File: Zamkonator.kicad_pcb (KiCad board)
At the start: 2 copper layers, 75 x 75 mm, 126 parts, among them J1 Screw_Terminal_01x06, J3 Conn_01x08_Male, J4 Conn_02x06_Counter_Clockwise, J5 Conn_01x04_Female, J6 Conn_01x03_Female, K1 SRD-DC3V-SL-C, Q1 BCP56, T1 HR051142, U1 RTL8201F, U2 SI3404-A-GM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

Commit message: Kicad updates, added missing resistances
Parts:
- C18: value C -> 100n 100V
- C21: value C -> 1n 100V
- R16: value R -> 130K
- R18: value R -> 0
- moved Q1 0.35 mm to (11.0, 27.6)
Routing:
- net Net-(U1-MDI0+): track 28.7 -> 26.2 mm

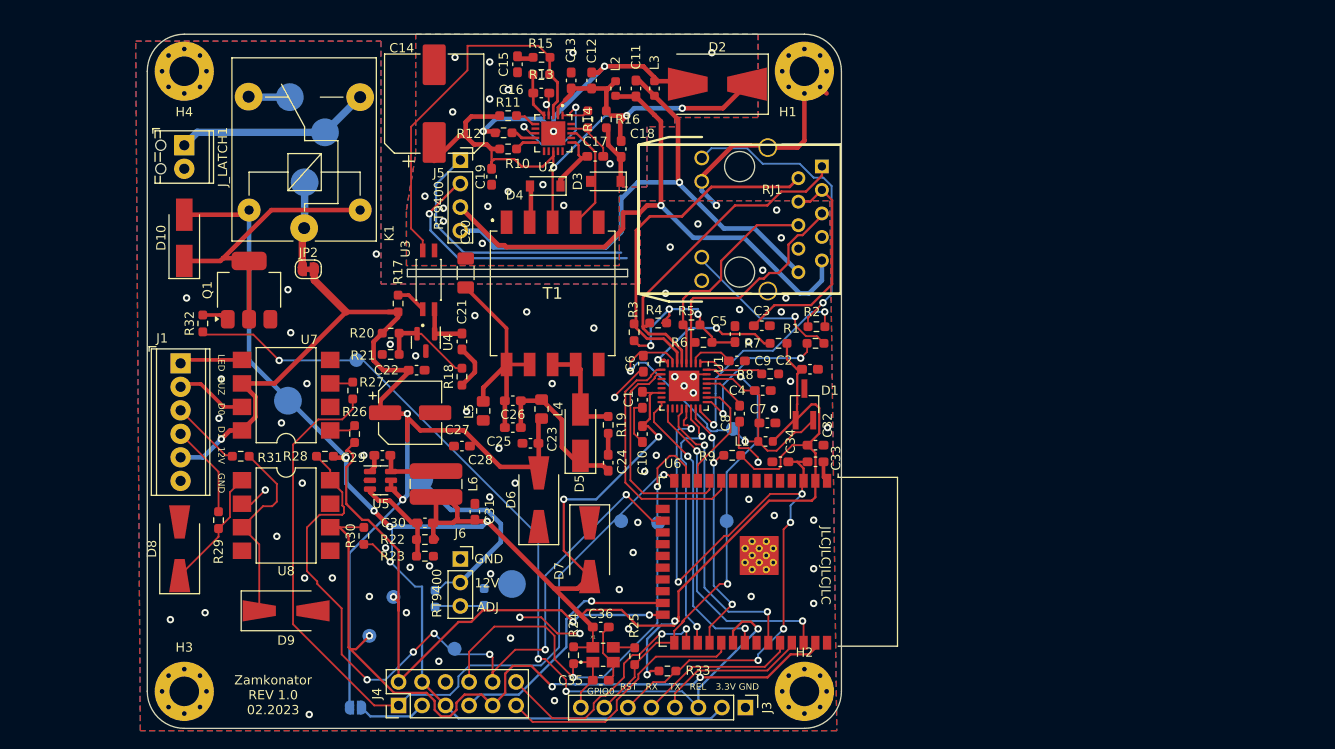
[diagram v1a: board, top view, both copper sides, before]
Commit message: Update schematic for V1.1
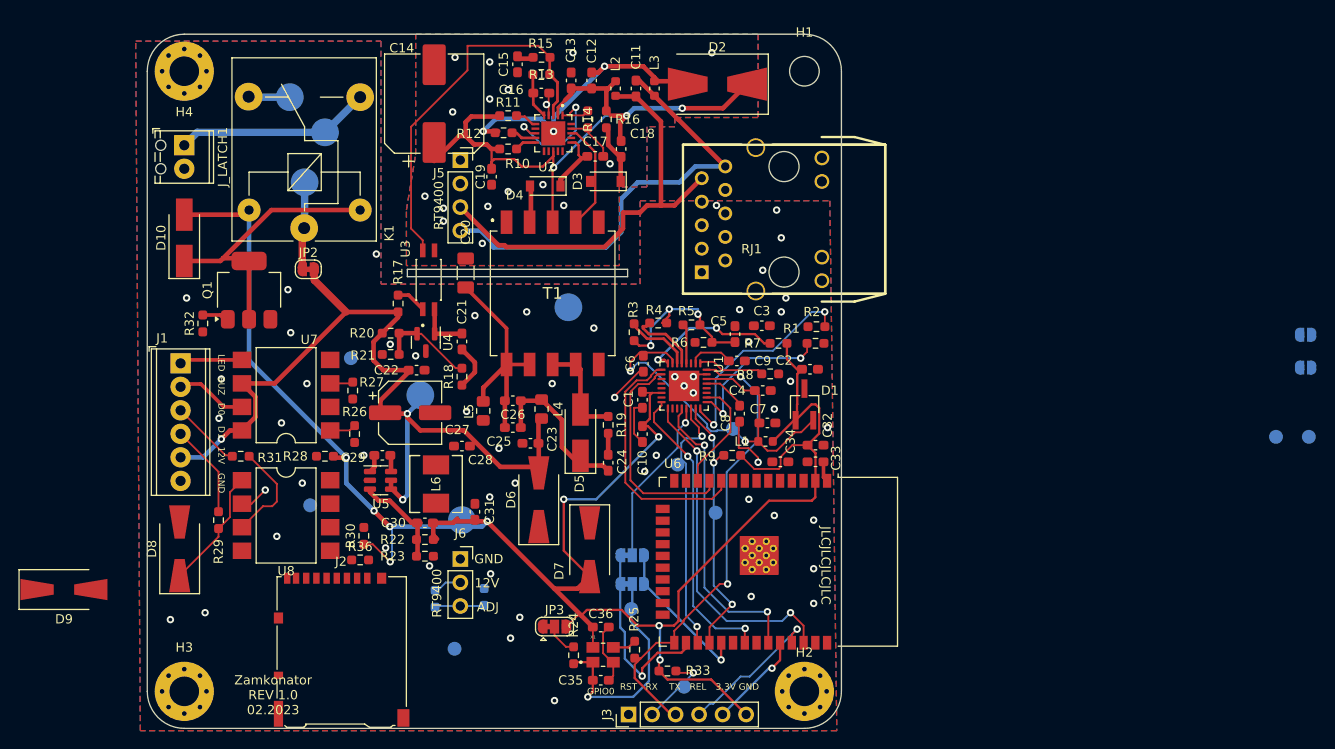
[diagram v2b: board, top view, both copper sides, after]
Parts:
- removed J4: Conn_02x06_Counter_Clockwise, Connector_PinHeader_2.54mm:PinHeader_2x06_P2.54mm_Vertical
- removed JP1: SolderJumper_2_Open, Jumper:SolderJumper-2_P1.3mm_Open_RoundedPad1.0x1.5mm
- added J2: Micro_SD_Card_Det1, Connector_Card:microSD_HC_Hirose_DM3AT-SF-PEJM5, F.Cu at (21.0, 66.5)
- added JP3: CLK_EN pull, Jumper:SolderJumper-3_P1.3mm_Bridged12_RoundedPad1.0x1.5mm, F.Cu at (44.0, 64.0)
- added JP4: EMAC_EN_JUMPER, Jumper:SolderJumper-3_P1.3mm_Bridged12_RoundedPad1.0x1.5mm, B.Cu at (52.4, 56.3)
- added JP5: CLK_EN_JUMPER, Jumper:SolderJumper-3_P1.3mm_Bridged12_RoundedPad1.0x1.5mm, B.Cu at (52.4, 59.4)
- added JP6: SolderJumper_2_Open, Jumper:SolderJumper-2_P1.3mm_Open_RoundedPad1.0x1.5mm, B.Cu at (125.2, 32.5)
- added JP7: SolderJumper_2_Open, Jumper:SolderJumper-2_P1.3mm_Open_RoundedPad1.0x1.5mm, B.Cu at (125.2, 36.0)
- added R36: 10k, Resistor_SMD:R_0603_1608Metric_Pad0.98x0.95mm_HandSolder, F.Cu at (23.0, 56.8)
- added TP15: EMAC_MDC, TestPoint:TestPoint_Pad_D1.5mm, B.Cu at (57.3, 46.5)
- added TP16: EMAC_MDIO, TestPoint:TestPoint_Pad_D1.5mm, B.Cu at (61.4, 51.7)
- H1: footprint MountingHole:MountingHole_3.2mm_M3_Pad_Via -> MountingHole:MountingHole_3.2mm_M3
- J3: footprint Connector_PinHeader_2.54mm:PinHeader_1x08_P2.54mm_Vertical -> Connector_PinHeader_2.54mm:PinHeader_1x06_P2.54mm_Vertical
- L6: value SWPA6045S6R8MT -> ETQP3M6R8KVP; footprint SWPA6045S6R8MT:SWPA6045S6R8MT -> panasonic_coil:IND_PCC-M0530M-LP_PAN
- R11: value 24.3 1% -> 24.3k 1%
- TP1: value TestPoint -> GND
- TP10: value TestPoint -> DAT0_INV
- TP11: value TestPoint -> LED_CTL
- TP12: value TestPoint -> R_NO
- TP13: value TestPoint -> R_NC
- TP14: value TestPoint -> R_C
- TP2: value TestPoint -> +12V
- TP3: value TestPoint -> ESP_EN
- TP4: value TestPoint -> RELAY_CTL
- TP5: value TestPoint -> PHY_AVDD
- TP6: value TestPoint -> +3.3V
- TP7: value TestPoint -> CLK_EN
- TP8: value TestPoint -> BUZZER_CTL
- TP9: value TestPoint -> DAT1_INV
- moved TP4 103.2 mm to (125.5, 43.5)
- moved TP11 100.3 mm to (122.0, 43.5)
- moved TP8 34.1 mm to (22.0, 35.0)
- moved TP1 30.5 mm to (45.5, 29.5)
- moved D9 24.1 mm to (-9.00, 60.0)
- moved TP6 22.8 mm to (34.0, 52.5)
- moved TP3 18.5 mm to (58.0, 70.5)
- moved TP10 13.4 mm to (17.6, 50.9)
- moved J3 12.6 mm to (52.0, 73.5), turned to 90 degrees
- moved TP7 9.74 mm to (52.3, 62.1)
- moved TP2 9.00 mm to (29.5, 39.0)
- moved R25 0.70 mm to (52.7, 66.5)
- turned RJ1 to 180 degrees
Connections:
- net /ESP32/EMAC_CRS_DV renamed /EMAC_CRS_DV
- net /ESP32/EMAC_MDC renamed /EMAC_MDC
- net /ESP32/EMAC_MDIO renamed /EMAC_MDIO
- net /ESP32/EMAC_RXD0 renamed /EMAC_RXD0
- net /ESP32/EMAC_RXD1 renamed /EMAC_RXD1
- net /ESP32/EMAC_TXD0 renamed /EMAC_TXD0
- net /ESP32/EMAC_TXD1 renamed /EMAC_TXD1
- net /ESP32/EMAC_TX_EN renamed /EMAC_TX_EN
- net /ESP32/IO12 renamed /BUZ_CTL
- net /ESP32/RX renamed /ESP_RX
- net /ESP32/TX renamed /ESP_TX
- C33 pad 1: /ESP32/ESP_EN -> /ESP_EN
- C34 pad 1: /ESP32/ESP_EN -> /ESP_EN
- C35 pad 1: /50MHZ CLOCK/CLK_EN -> /CLK_EN
- J3 pad 2: +3.3V -> /ESP_EN
- J3 pad 3: /ESP32/IO18 -> /ESP_IO0
- J3 pad 6: /ESP32/ESP_EN -> +3.3V
- R24 pad 1: +3.3V -> Net-(JP3-C)
- R24 pad 2: /50MHZ CLOCK/CLK_EN -> /CLK_EN
- R25 pad 2: /50MHZ CLOCK/CLK_OUT -> /ESP_IO0
- R26 pad 1: /ESP32/IO2 -> /LED_CTL
- R28 pad 2: /ESP32/IO13 -> /DAT1_INV
- R30 pad 2: /ESP32/IO23 -> /DAT0_INV
- R32 pad 1: /ESP32/IO18 -> /RELAY_CTL
- R33 pad 2: /ESP32/ESP_EN -> /ESP_EN
- TP10 pad 1: /ESP32/IO2 -> /DAT1_INV
- TP11 pad 1: /ESP32/IO23 -> /LED_CTL
- TP3 pad 1: /50MHZ CLOCK/CLK_OUT -> /ESP_EN
- TP4 pad 1: /ESP32/IO18 -> /RELAY_CTL
- TP7 pad 1: /50MHZ CLOCK/CLK_EN -> /CLK_EN
- TP9 pad 1: /ESP32/IO13 -> /DAT0_INV
- U1 pad 21: /ESP32/ESP_EN -> /EMAC_EN
- U1 pad 32: /50MHZ CLOCK/CLK_OUT -> /ESP_IO0
- U6 pad 13: /50MHZ CLOCK/CLK_EN -> /IO14
- U6 pad 16: /ESP32/IO13 -> /IO13
- U6 pad 23: /ESP32/IO15 -> /IO15
- U6 pad 24: /ESP32/IO2 -> /IO2
- U6 pad 25: /50MHZ CLOCK/CLK_OUT -> /ESP_IO0
- U6 pad 26: /ESP32/IO4 -> /IO4
- U6 pad 29: /ESP32/IO5 -> /IO5
- U6 pad 3: /ESP32/ESP_EN -> /ESP_EN
- U6 pad 30: /ESP32/IO18 -> /RELAY_CTL
- U6 pad 37: /ESP32/IO23 -> /LED_CTL
- U6 pad 6: unconnected-(U6-IO34-Pad6) -> /DAT0_INV
- U6 pad 7: unconnected-(U6-IO35-Pad7) -> /DAT1_INV
- U8 pad 6: /ESP32/IO23 -> /DAT0_INV
- U8 pad 8: /ESP32/IO13 -> /DAT1_INV
- X1 pad 1: /50MHZ CLOCK/CLK_EN -> /CLK_EN
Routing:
- net /ESP32/IO18: track 94.8 -> 0.00 mm, vias 4 -> 0
- net /BUZ_CTL: track 89.1 -> 0.00 mm, vias 1 -> 0
- net /ESP32/IO13: track 83.7 -> 0.00 mm, vias 6 -> 0
- net /ESP32/IO23: track 82.9 -> 0.00 mm, vias 3 -> 0
- net /ESP32/ESP_EN: track 80.3 -> 0.00 mm, vias 6 -> 0
- net /ESP32/IO2: track 64.0 -> 0.00 mm, vias 3 -> 0
- net /50MHZ CLOCK/CLK_EN: track 62.4 -> 0.00 mm, vias 2 -> 0
- net /ESP_IO0: track 0.00 -> 51.4 mm, vias 0 -> 2
- net /50MHZ CLOCK/CLK_OUT: track 49.5 -> 0.00 mm, vias 2 -> 0
- net +3.3V: track 266.8 -> 217.7 mm
- net +12V: track 145.8 -> 100.2 mm
- net GND: track 71.1 -> 36.2 mm, vias 70 -> 55
- net Net-(R2-Pad1): track 32.4 -> 0.00 mm, vias 1 -> 0
- net Net-(U1-MDI1-): track 37.2 -> 6.76 mm
- net unconnected-(J5-Pin_1-Pad1): track 29.3 -> 0.00 mm
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
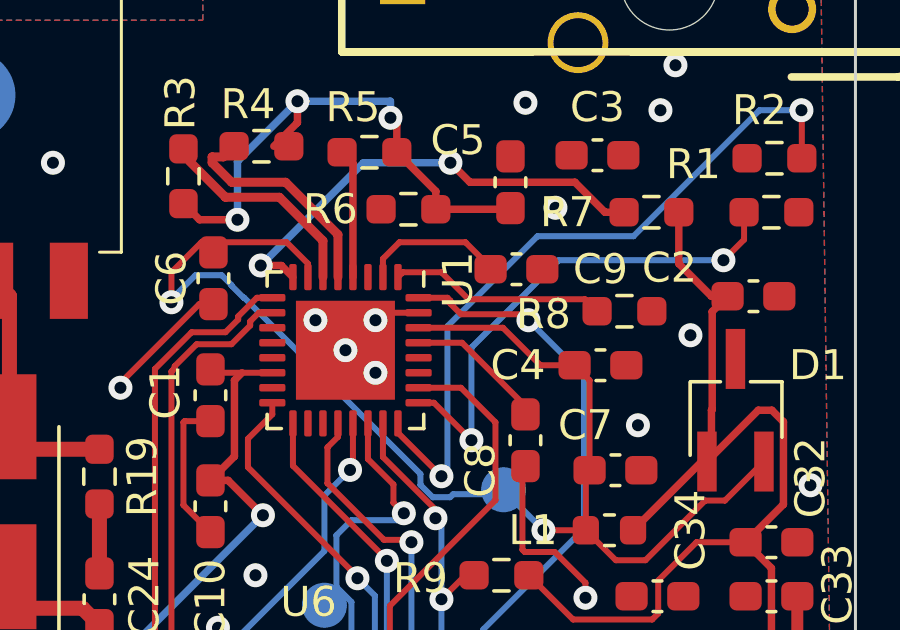
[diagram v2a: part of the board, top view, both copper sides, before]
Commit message: use contributed symbol for RTL8021F
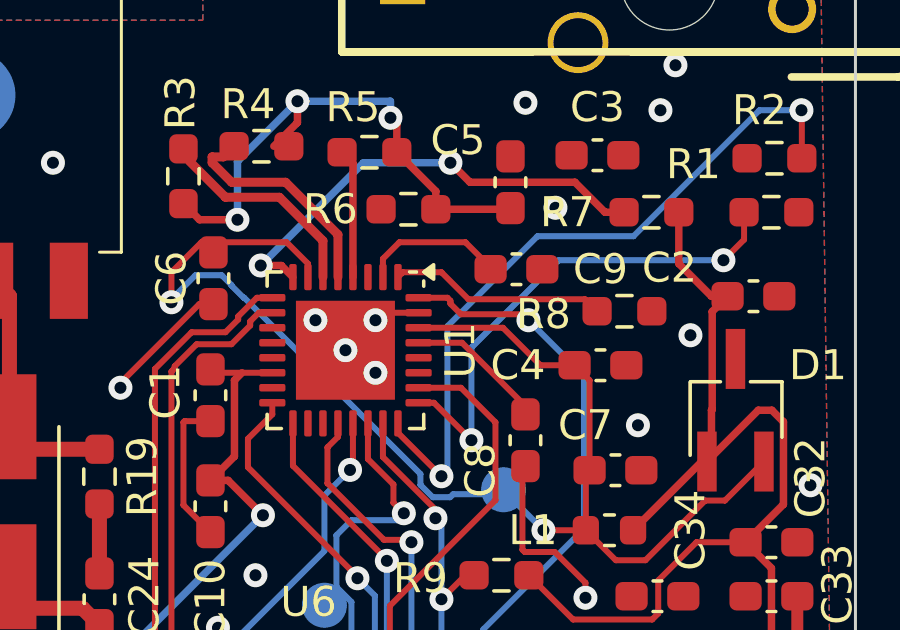
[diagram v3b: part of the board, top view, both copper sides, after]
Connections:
- C4 pad 2: GND -> Net-(C4-Pad2)
- C6 pad 2: GND -> Net-(C4-Pad2)
- C7 pad 2: GND -> Net-(C4-Pad2)
- R1 pad 2: Net-(U1-LED1/PHYAD1) -> Net-(U1-LED0/PHYAD1/PMEB)
- R2 pad 2: Net-(U1-LED0/PHYAD0) -> Net-(U1-LED1/PHYAD1)
- U1 pad 24: Net-(U1-LED0/PHYAD0) -> Net-(U1-LED0/PHYAD1/PMEB)
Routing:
- net Net-(U1-LED0/PHYAD0): track 23.8 -> 0.00 mm, vias 2 -> 0
- net Net-(U1-LED0/PHYAD1/PMEB): track 0.00 -> 16.9 mm, vias 0 -> 2
- net Net-(U1-LED1/PHYAD1): track 16.9 -> 23.8 mm
- net GND: track 36.2 -> 31.9 mm
- net Net-(C4-Pad2): track 0.00 -> 4.35 mm

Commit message: BOM updates & schematic fixes
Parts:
- added TP17: POE+, TestPoint:TestPoint_Pad_D1.5mm, B.Cu at (34.5, 6.50)
- added TP18: POE-, TestPoint:TestPoint_Pad_D1.5mm, B.Cu at (37.5, 5.00)
- added TP19: VT15, TestPoint:TestPoint_Pad_D1.5mm, B.Cu at (46.5, 15.0)
- added TP20: EROUT, TestPoint:TestPoint_Pad_D1.5mm, B.Cu at (30.2, 20.0)
- added TP21: FBH, TestPoint:TestPoint_Pad_D1.5mm, B.Cu at (30.8, 15.5)
- added TP22: OPTO_IN, TestPoint:TestPoint_Pad_D1.5mm, B.Cu at (33.5, 29.8)
- added TP23: VSS, TestPoint:TestPoint_Pad_D1.5mm, B.Cu at (63.5, 2.25)
- moved TP4 122.9 mm to (3.25, 31.0)
- moved JP6 112.9 mm to (16.0, 61.4), turned to -90 degrees
- moved JP7 104.5 mm to (23.8, 61.4), turned to -90 degrees
- moved TP11 53.4 mm to (72.2, 63.0)
- moved TP9 21.1 mm to (16.5, 53.5)
- moved D9 18.5 mm to (9.25, 62.8), turned to -90 degrees
- moved TP10 0.86 mm to (16.8, 51.0)
- moved R9 0.50 mm to (63.2, 46.0)
- moved C1 0.25 mm to (53.5, 39.8)
- moved C28 0.25 mm to (34.0, 44.2)
- moved C6 0.10 mm to (53.6, 35.5)
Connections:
- C4 pad 2: Net-(C4-Pad2) -> GND
- C6 pad 2: Net-(C4-Pad2) -> GND
- C7 pad 2: Net-(C4-Pad2) -> GND
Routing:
- net /RELAY_CTL: track 0.00 -> 105.2 mm, vias 0 -> 3
- net /LED_CTL: track 0.00 -> 98.1 mm, vias 0 -> 5
- net /DAT1_INV: track 0.00 -> 61.3 mm, vias 0 -> 3
- net /DAT0_INV: track 0.00 -> 58.5 mm, vias 0 -> 5
- net /BUZ_CTL: track 0.00 -> 51.6 mm, vias 0 -> 3
- net /IO14: track 0.00 -> 50.8 mm, vias 0 -> 2
- net /IO2: track 0.00 -> 41.9 mm, vias 0 -> 2
- net /IO15: track 0.00 -> 37.5 mm, vias 0 -> 2
- net /IO13: track 0.00 -> 37.4 mm, vias 0 -> 2
- net /ESP_EN: track 8.32 -> 43.1 mm, vias 1 -> 2
- net +3.3V: track 217.7 -> 247.7 mm
- net +12V: track 100.2 -> 120.3 mm
- net Net-(R1-Pad1): track 0.00 -> 18.3 mm
- net Net-(U1-MDI+0): track 0.00 -> 15.8 mm
- net Net-(U1-MDI-0): track 4.31 -> 19.9 mm
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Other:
- board text added: "IO0"
- board text added: "Zamkonator REV 1.1 06.2025"
- board text removed: "CLK_EN"
- board text removed: "COM"
- board text removed: "GPIO0"
- board text removed: "IO12"
- board text removed: "IO13"
- board text removed: "IO23"
- board text removed: "NC"
- board text removed: "NO"
- board text removed: "REL"
- board text removed: "RELAY"
- board text removed: "Zamkonator REV 1.0 02.2023"

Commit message: DO the bulk of rev 1.2 layout
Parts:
- removed JP2: SolderJumper_2_Bridged, Jumper:SolderJumper-2_P1.3mm_Bridged_RoundedPad1.0x1.5mm
- removed JP3: CLK_EN pull, Jumper:SolderJumper-3_P1.3mm_Bridged12_RoundedPad1.0x1.5mm
- removed JP4: EMAC_EN_JUMPER, Jumper:SolderJumper-3_P1.3mm_Bridged12_RoundedPad1.0x1.5mm
- removed JP5: CLK_EN_JUMPER, Jumper:SolderJumper-3_P1.3mm_Bridged12_RoundedPad1.0x1.5mm
- removed J_LATCH1: Screw_Terminal_01x02, TerminalBlock_Phoenix:TerminalBlock_Phoenix_MPT-0,5-2-2.54_1x02_P2.54mm_Horizontal
- added D11: PESD15VL1BA, Diode_SMD:D_SOD-323, F.Cu at (3.50, 30.5)
- added D12: PESD15VL1BA, Diode_SMD:D_SOD-323, F.Cu at (3.45, 26.0)
- added D13: PESD15VL1BA, Diode_SMD:D_SOD-323, F.Cu at (3.50, 28.2)
- added D9: PESD5V0L1BA, Diode_SMD:D_SOD-323, F.Cu at (3.50, 53.8)
- added J4: Screw_Terminal_01x06, TerminalBlock_Phoenix:TerminalBlock_Phoenix_MPT-0,5-6-2.54_1x06_P2.54mm_Horizontal, F.Cu at (3.60, 10.3)
- added R37: 100K 1%, Resistor_SMD:R_0603_1608Metric_Pad0.98x0.95mm_HandSolder, F.Cu at (17.0, 28.7)
- added U10: EL3H7-G, project specific:SOIC127P700X200-4N, F.Cu at (14.0, 47.4)
- added U9: EL3H7-G, project specific:SOIC127P700X200-4N, F.Cu at (14.0, 36.2)
- D6: value 12V -> PESD15VL1BA; footprint Diode_SMD:D_SMA-SMB_Universal_Handsoldering -> Diode_SMD:D_SOD-323
- D7: value 3.3 -> PESD3V3L1BA; footprint Diode_SMD:D_SMA-SMB_Universal_Handsoldering -> Diode_SMD:D_SOD-323
- D8: value 5V5 -> PESD5V0L1BA; footprint Diode_SMD:D_SMA-SMB_Universal_Handsoldering -> Diode_SMD:D_SOD-323
- Q1: value BCP56 -> DMG2302U; footprint Package_TO_SOT_SMD:SOT-223-3_TabPin2 -> Package_TO_SOT_SMD:SOT-23
- R32: value R -> 1k
- U7, U8: value LTV-827S -> EL3H7-G; footprint Package_DIP:SMDIP-8_W9.53mm -> project specific:SOIC127P700X200-4N
- moved C29 19.7 mm to (42.8, 54.8)
- moved C3 16.2 mm to (55.5, 19.5), turned to 180 degrees
- moved U5 14.8 mm to (39.0, 53.5), turned to 90 degrees
- moved R7 14.7 mm to (53.5, 33.2), turned to 90 degrees
- moved D10 14.4 mm to (18.0, 25.1), turned to 180 degrees
- moved R31 13.8 mm to (6.75, 32.2)
- moved R23 13.7 mm to (42.8, 51.4)
- moved L6 13.6 mm to (39.2, 59.5), turned to -90 degrees
- moved C33 13.5 mm to (59.5, 41.8)
- moved C30 13.1 mm to (42.8, 49.8)
- moved R22 12.8 mm to (42.8, 53.1)
- moved TP4 12.8 mm to (16.0, 32.2)
- moved R30 11.9 mm to (20.2, 42.8), turned to 180 degrees
- moved C31 11.8 mm to (45.5, 57.8), turned to 0 degrees
- moved D6 11.5 mm to (31.2, 47.2)
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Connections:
- net Net-(C4-Pad1) renamed /Ethenet PHY/PHY_AVDD
- D10 pad 1: Net-(D10-K) -> +3.3V
- D10 pad 2: +3.3V -> Net-(D10-A)
- D8 pad 1: Net-(D8-A1) -> GND2
- D8 pad 2: GND -> Net-(D8-A2)
- D9 pad 2: GND -> GND2
- H4 pad 1: GND -> GND2
- J1 pad 5: +12V -> /EXT_PWR
- J1 pad 6: GND -> GND2
- K1 pad 2: Net-(D10-K) -> +3.3V
- K1 pad 5: +3.3V -> Net-(D10-A)
- Q1 pad 2: Net-(D10-K) -> GND
- Q1 pad 3: GND -> Net-(D10-A)
- R24 pad 1: Net-(JP3-C) -> /CLK_EN
- R24 pad 2: /CLK_EN -> GND
- R29 pad 1: Net-(D8-A1) -> Net-(D8-A2)
- R31 pad 1: Net-(D9-A1) -> Net-(D9-A2)
- T1 pad 3: Net-(D2-K) -> Net-(D3-A)
- T1 pad 4: Net-(D3-A) -> Net-(D2-K)
- U1 pad 21: /EMAC_EN -> /CLK_EN
- U6 pad 26: /IO4 -> /CLK_EN
- U7 pad 1: Net-(R26-Pad2) -> Net-(R27-Pad2)
- U7 pad 3: Net-(R27-Pad2) -> /Wigand Intrerface/READER_BUZZER
- U7 pad 4: GND -> /Wigand Intrerface/EXT_PWR
- U8 pad 1: Net-(D8-A1) -> Net-(D9-A2)
- U8 pad 2: GND -> GND2
- U8 pad 3: Net-(D9-A1) -> GND
- U8 pad 4: GND -> /DAT0_INV
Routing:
- net +3.3V: track 247.7 -> 65.3 mm, vias 9 -> 2
- net /RELAY_CTL: track 105.2 -> 1.88 mm, vias 3 -> 0
- net /LED_CTL: track 98.1 -> 0.00 mm, vias 5 -> 0
- net /DAT1_INV: track 61.3 -> 0.00 mm, vias 3 -> 0
- net /DAT0_INV: track 58.5 -> 0.00 mm, vias 5 -> 0
- net /BUZ_CTL: track 51.6 -> 0.00 mm, vias 3 -> 0
- net /IO14: track 50.8 -> 0.00 mm, vias 2 -> 0
- net +12V: track 120.3 -> 69.8 mm, vias 3 -> 0
- net /IO2: track 41.9 -> 0.00 mm, vias 2 -> 0
- net /IO13: track 37.4 -> 0.00 mm, vias 2 -> 0
- net /IO15: track 37.5 -> 3.45 mm, vias 2 -> 0
- net /RT9400_VB1: track 47.1 -> 13.9 mm
- net Net-(D10-K): track 30.6 -> 0.00 mm
- net /IO4: track 21.1 -> 0.00 mm, vias 1 -> 0
- net /EMAC_EN: track 18.9 -> 0.00 mm, vias 1 -> 0
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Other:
- outline, holes or cut-outs redrawn
- board text added: "Zamkonator REV 1.2 09.2025"
- board text removed: "Zamkonator REV 1.1 06.2025"
